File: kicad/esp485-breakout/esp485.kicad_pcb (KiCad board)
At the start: 2 copper layers, 25.4 x 22.9 mm, 15 parts, among them J1 Conn_01x07, J2 Conn_01x07, SW1 SW_Push, SW2 SW_Push, U1 MAX3485, U2 ESP-WROOM-02

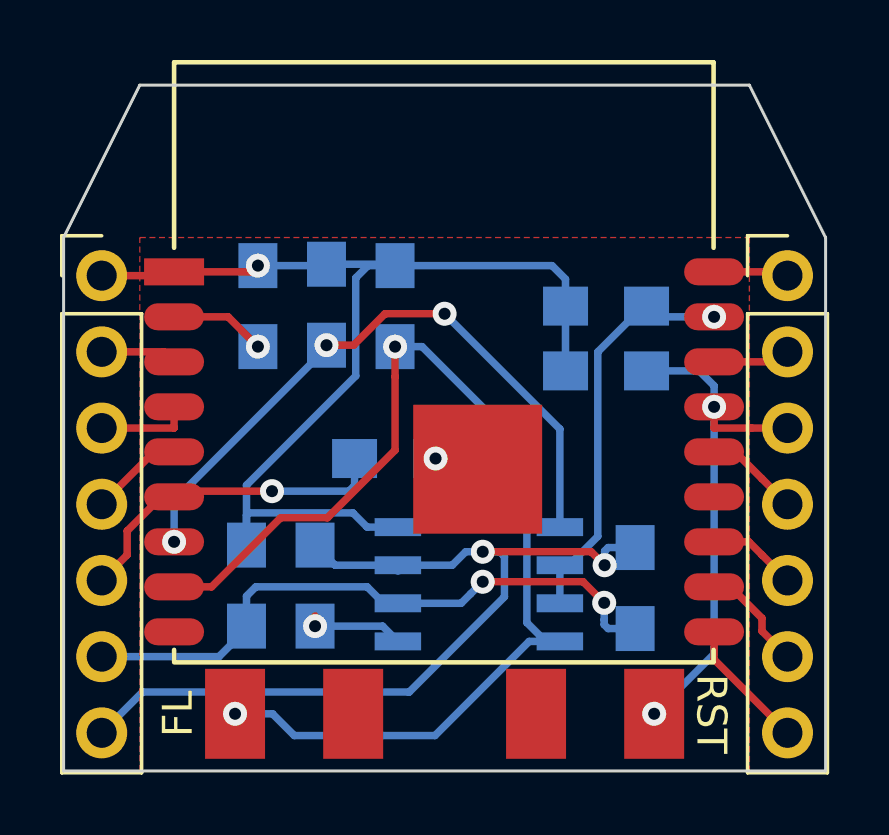
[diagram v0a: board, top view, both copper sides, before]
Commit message: stop using modules from github to enable 3d models
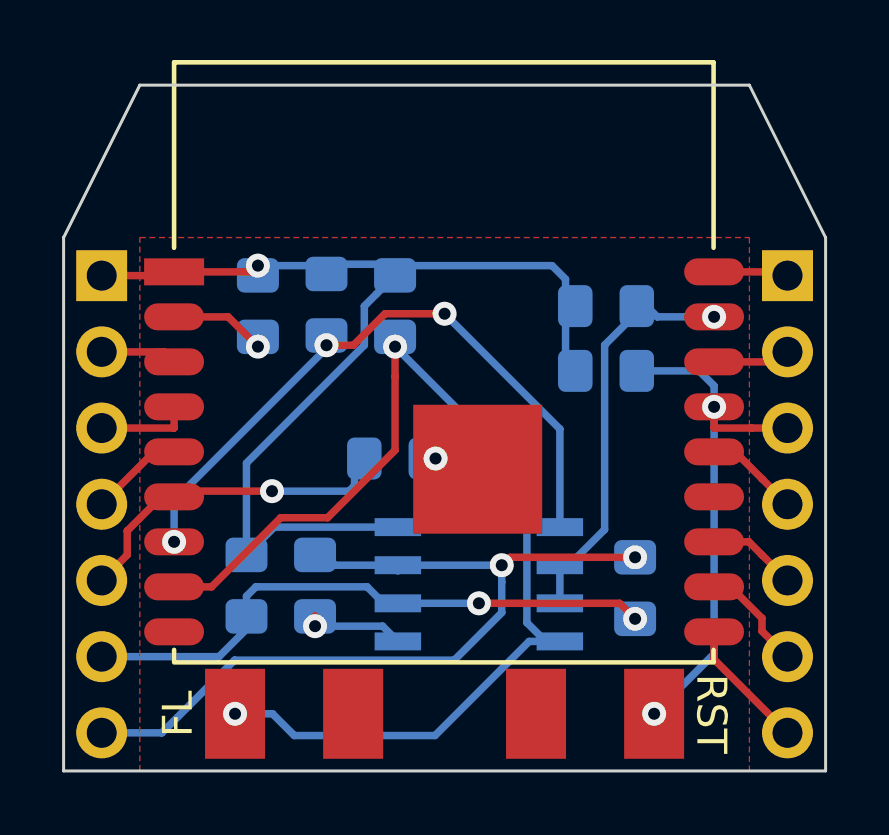
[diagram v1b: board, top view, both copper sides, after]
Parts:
- J1, J2: footprint Pin_Headers:Pin_Header_Straight_1x07_Pitch2.54mm -> Connector_PinHeader_2.54mm:PinHeader_1x07_P2.54mm_Vertical; moved to B.Cu
- R1, R10, R2, R3, R4, R5, R7, R8, R9: footprint Resistors_SMD:R_0805_HandSoldering -> Resistor_SMD:R_0805_2012Metric_Pad1.15x1.40mm_HandSolder
- U1: footprint Housings_SOIC:SOIC-8_3.9x4.9mm_Pitch1.27mm -> Package_SO:SOIC-8_3.9x4.9mm_P1.27mm
- turned J1 to 180 degrees
- turned J2 to 180 degrees
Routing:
- net Net-(J1-Pad7): track 29.5 -> 27.8 mm
- net +3V3: track 37.1 -> 35.7 mm
- net Net-(J1-Pad6): track 20.5 -> 19.4 mm
- net Net-(R3-Pad1): track 38.0 -> 37.5 mm

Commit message: rj45 update
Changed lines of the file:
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@@
     (mod_text_size 1 1)
     (mod_text_width 0.15)
-    (pad_size 2 0.9)
-    (pad_drill 0)
+    (pad_size 1.7 1.7)
+    (pad_drill 1)
     (pad_to_mask_clearance 0)
     (aux_axis_origin 0 0)
@@
     (pad 2 thru_hole oval (at 0 -2.54 180) (size 1.7 1.7) (drill 1) (layers *.Cu *.Mask)
       (net 8 "Net-(J2-Pad2)"))
-    (pad 1 thru_hole rect (at 0 0 180) (size 1.7 1.7) (drill 1) (layers *.Cu *.Mask)
+    (pad 1 thru_hole circle (at 0 0 180) (size 1.7 1.7) (drill 1) (layers *.Cu *.Mask)
       (net 6 GND))
     (model ${KISYS3DMOD}/Connector_PinHeader_2.54mm.3dshapes/PinHeader_1x07_P2.54mm_Vertical.wrl
